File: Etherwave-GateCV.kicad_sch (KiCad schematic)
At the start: 38 parts, among them J1 Etherwave Brd, J2 Volume CV, J3 Pitch CV, J4 Gate, Q1 PMP4501Y, Q2 PMBT3906, Q3 PMP4501Y, U1 LM13700, U2 CD4093, U3 CD4093, U4 4022, U5 TL072, U6 4016, U7 TL072

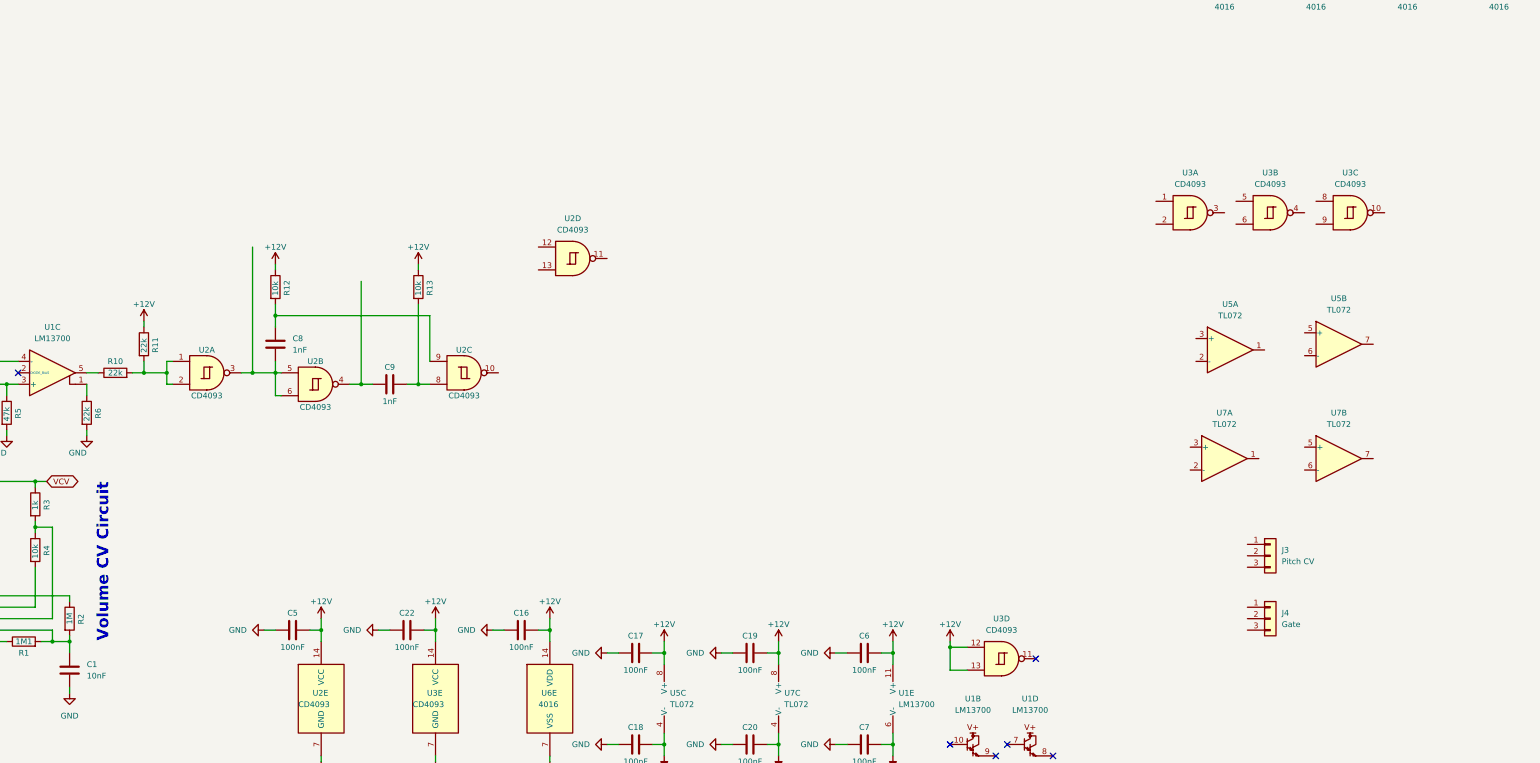
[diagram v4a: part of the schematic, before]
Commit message: completed pulse discriminator network
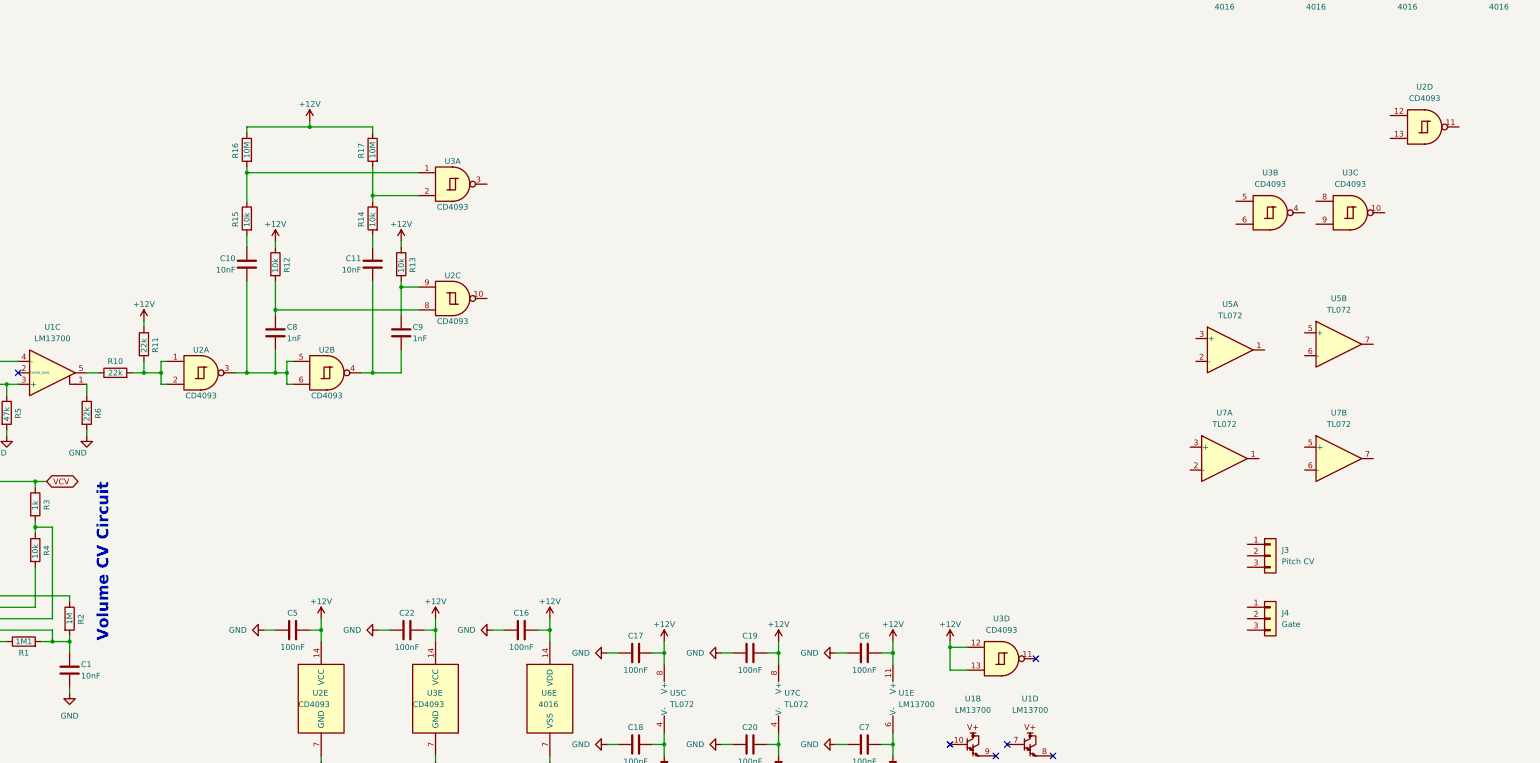
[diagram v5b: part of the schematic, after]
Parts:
- added C10, C11: 10nF, symbol Device:C
- added R14, R15: 10k, symbol Device:R
- added R16, R17: 10M, symbol Device:R
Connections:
- net +12V: now also R16.1, R17.1
- net at C8.1, R12.2: now also U2.8; no longer U2.9
- net at U2.4: now also C9.2, C11.2; no longer C9.1
- net at C8.2, U2.3, U2.5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: now also C10.2
- net at U3.1: now also R15.1, R16.2
- net at U3.2: now also R14.1, R17.2
- new net: C10.1, R15.2
- new net: C9.1, R13.2, U2.9
- new net: C11.1, R14.2
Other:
- moved on the sheet: C8, R12, R13, U2A, U2B, U2C, U2D, U3A

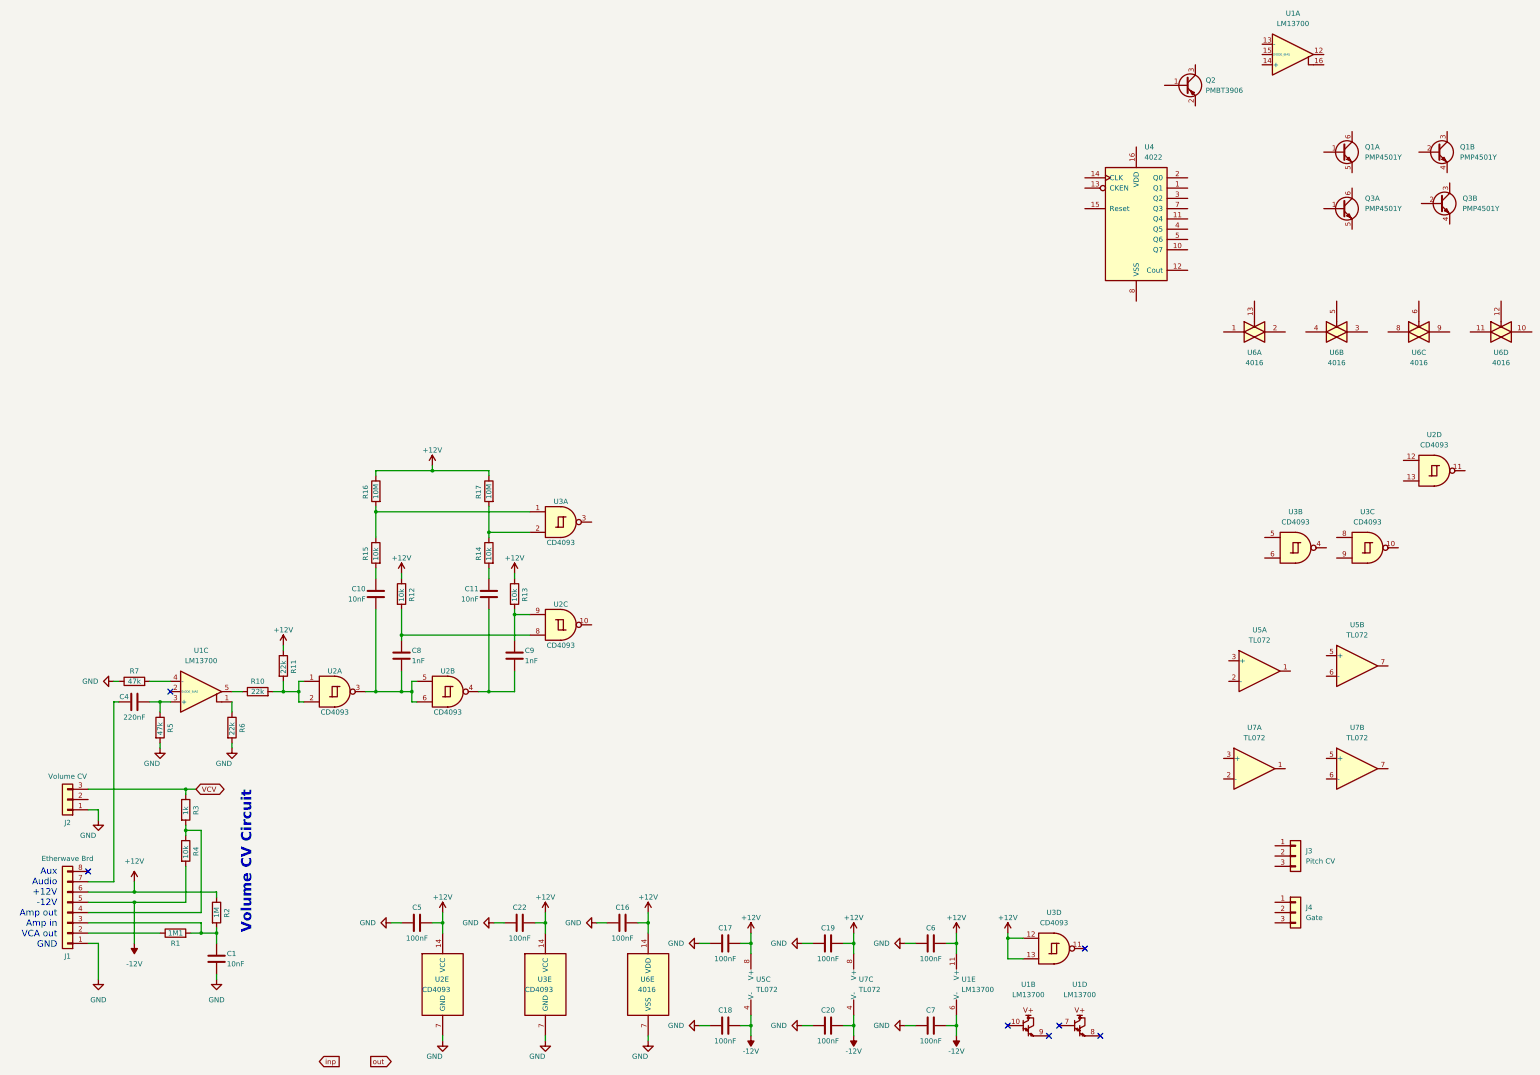
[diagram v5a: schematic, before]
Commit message: completed gate circuit
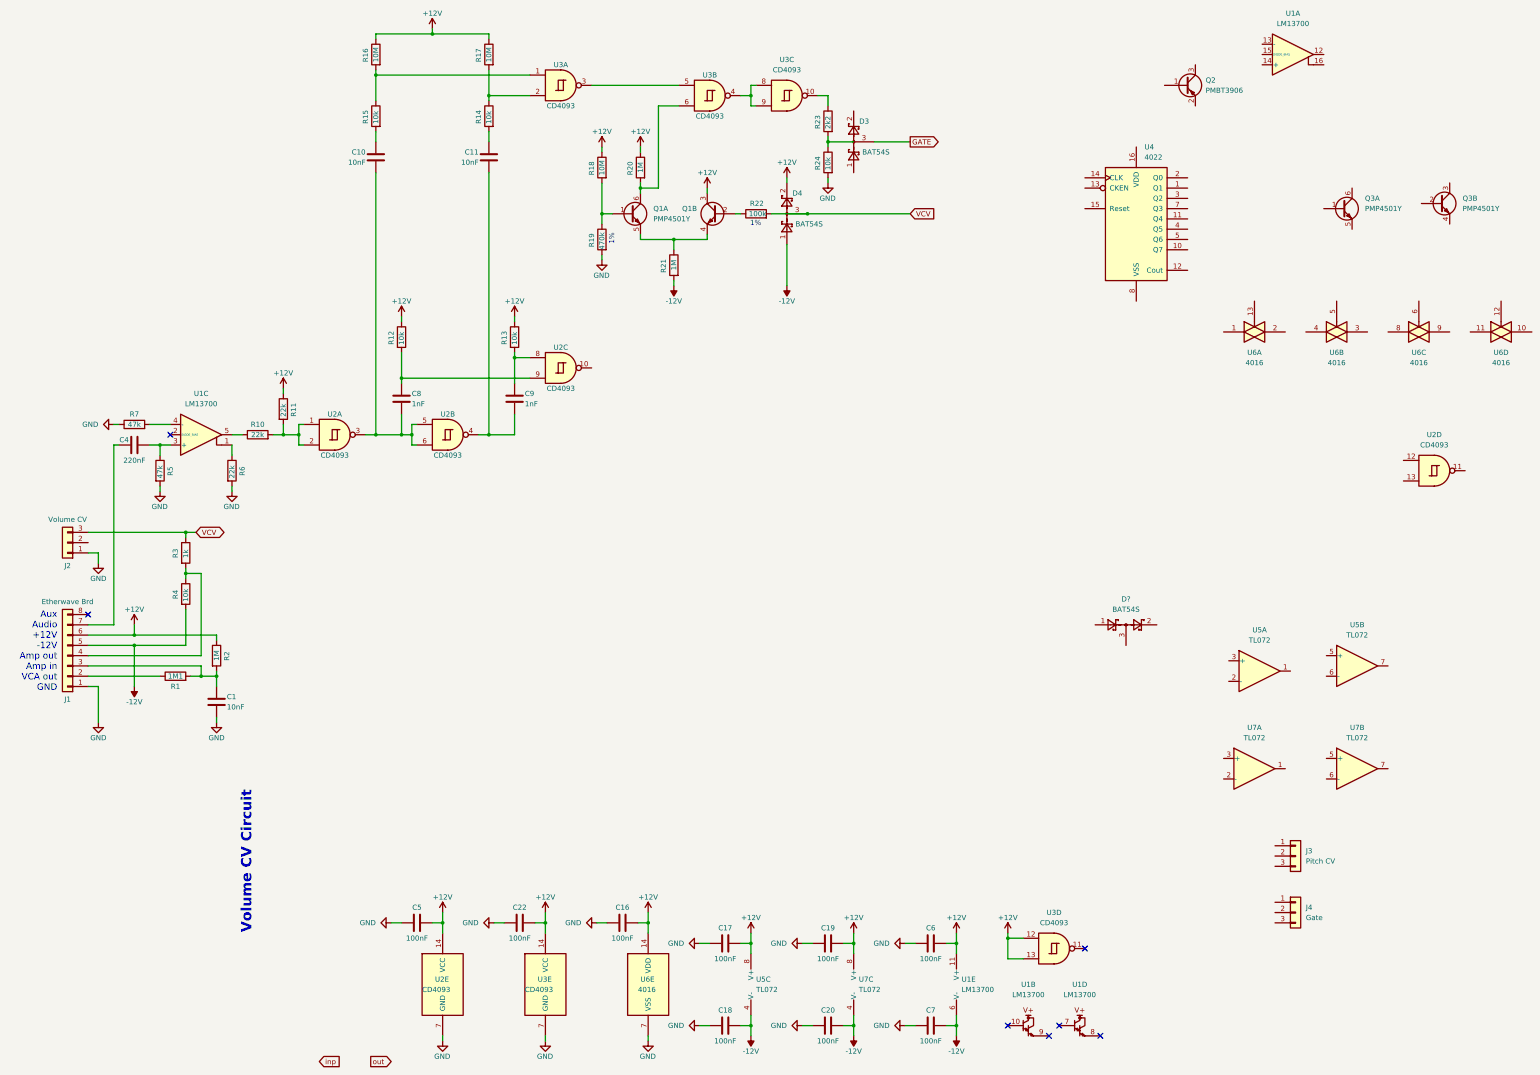
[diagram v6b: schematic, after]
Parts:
- added D3, D4, D?: BAT54S, Package_TO_SOT_SMD:SOT-23, symbol Diode:BAT54S
- added R18: 10M, symbol Device:R
- added R19: 470k, symbol Device:R
- added R20, R21: 1M, symbol Device:R
- added R22: 100k, symbol Device:R
- added R23: 2k2, symbol Device:R
- added R24: 10k, symbol Device:R
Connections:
- net +12V: now also Q1.3 (C2), D4.2, R18.1, R20.1
- net -12V: now also D4.1, R21.2
- net GND: now also R19.2, R24.2
- net VCV: now also D4.3, R22.2
- net at C8.1, R12.2: now also U2.9; no longer U2.8
- net at Q1.2 (B2): now also R22.1
- net at Q1.4 (E2): now also Q1.5 (E1), R21.1
- net at C9.1, R13.2: now also U2.8; no longer U2.9
- net at Q1.1 (B1): now also R18.2, R19.1
- net at Q1.6 (C1): now also U3.6, R20.2
- net at U3.3: now also U3.5
- net at U3.10: now also R23.1
- net at U3.8: now also U3.4, U3.9
- new net: R23.2, R24.1
- new net GATE: D3.3
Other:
- note added: "1%"
- moved on the sheet: C1, C10, C11, C4, C8, C9, J1, J2, Q1A, Q1B, R1, R10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

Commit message: replaced circuits
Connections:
- net GATE is gone; now on an unnamed net: D3.3
- net +12V: now also D3.2, R2.2; no longer R2.1
- net -12V: now also R4.1; no longer D4.1, R4.2
- net GND: now also D3.1, D4.1, J4.1 (Pin_1)
- net at J4.3 (Pin_3): now also R23.2, R24.1
- net at C1.1, J1.3 (Pin_3), R1.2: now also R2.1; no longer R2.2
- net VCV: no longer names the net of D4.3, J2.3 (Pin_3), R22.2
- net VCV: now also R3.2; no longer R3.1
- new net: J1.4 (Pin_4), R3.1, R4.2
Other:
- note added: "Volume CV"
- note removed: "Volume CV Circuit"
- moved on the sheet: C1, C10, C11, C4, C8, C9, D3, D4, D?, J1, J2, J3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

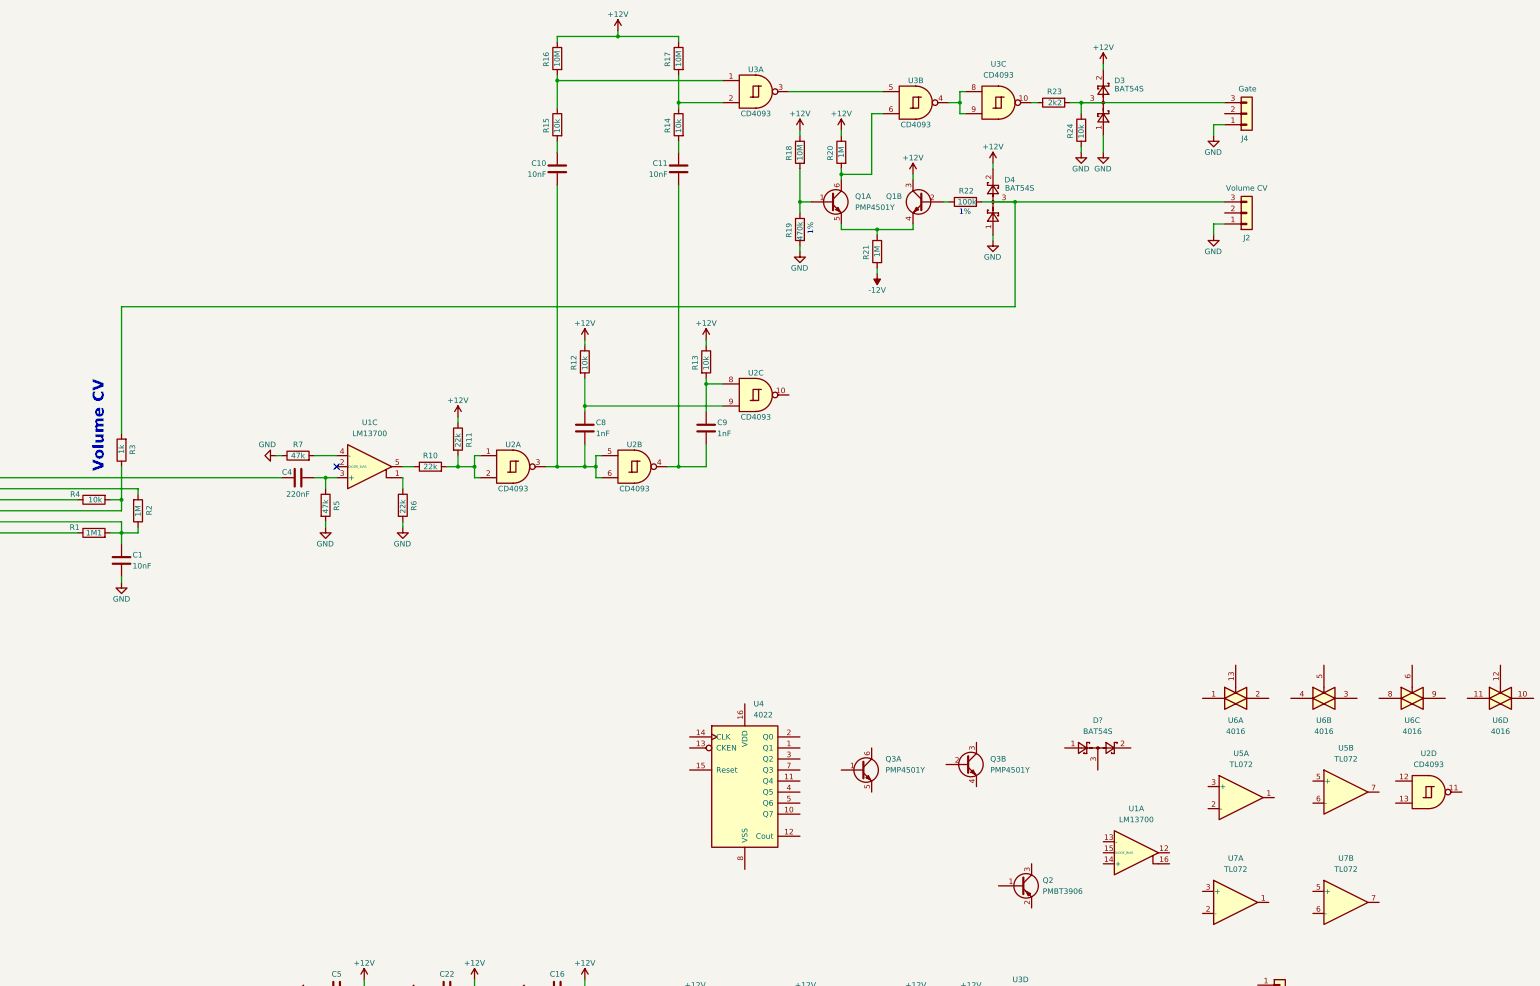
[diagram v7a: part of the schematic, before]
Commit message: completed counter circuit
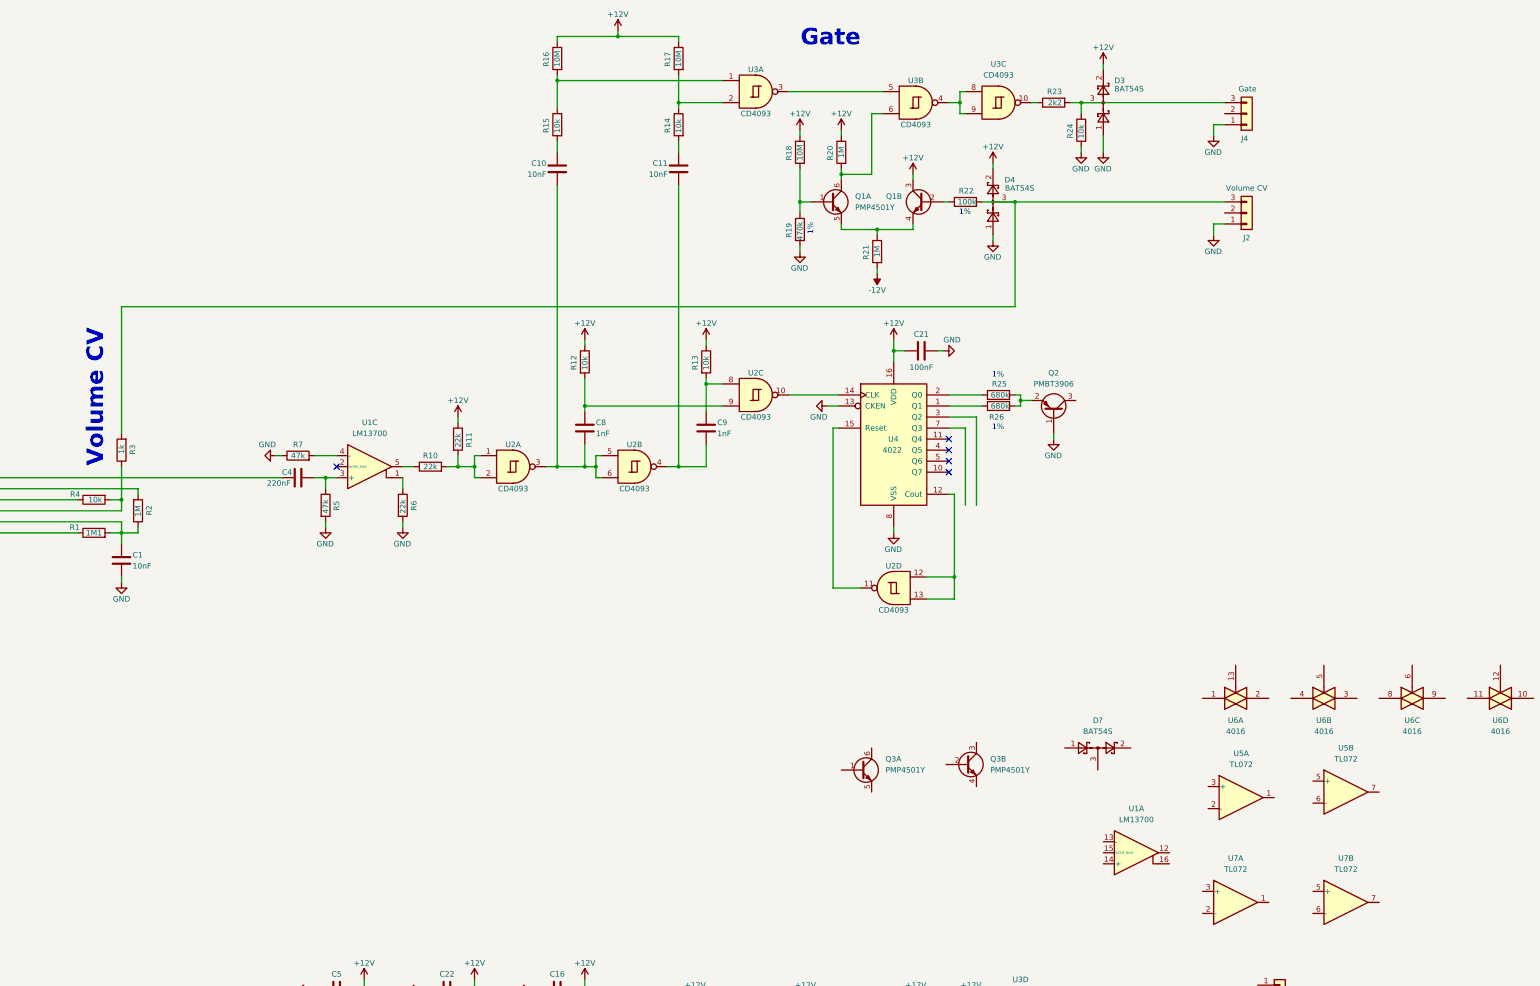
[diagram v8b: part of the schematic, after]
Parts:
- added C21: 100nF, symbol Device:C
- added R25, R26: 680k, symbol Device:R
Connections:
- net +12V: now also U4.16 (VDD), C21.2
- net GND: now also Q2.1 (B), U4.13 (CKEN), U4.8 (VSS), C21.1
- net at U2.10: now also U4.14 (CLK)
- net at Q2.2 (E): now also R25.2, R26.2
- net at U4.1 (Q1): now also R26.1
- net at U4.12 (Cout): now also U2.12, U2.13
- net at U4.15 (Reset): now also U2.11
- net at U4.2 (Q0): now also R25.1
- no-connect marks 7 -> 11
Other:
- note added: "Gate"
- moved on the sheet: Q2, U2D, U4
